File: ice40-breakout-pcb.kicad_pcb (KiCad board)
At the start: 2 copper layers, 55 parts, among them J1 USB_B_Micro, J2 USB_Break_Out, U1 SIT2001BI-S2-33E-12.000000G, U2 TLV73333PDBV, U3 TLV73312PDBV, U4 AT25SF081-SHD-X, U5 ICE40HX4K-TQ144

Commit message: Experimenting with external connector configuration.
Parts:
- added J3: Conn_02x16_Odd_Even, Connector_PinHeader_2.54mm:PinHeader_2x16_P2.54mm_Vertical, F.Cu at (94.8, 66.6)
- added J4: Conn_02x16_Odd_Even, Connector_PinHeader_2.54mm:PinHeader_2x16_P2.54mm_Vertical, F.Cu at (145.2, 104.7)
- added J5: Conn_02x16_Odd_Even, Connector_PinHeader_2.54mm:PinHeader_2x16_P2.54mm_Vertical, F.Cu at (139.1, 60.5)
- added J6: Conn_02x04_Odd_Even, Connector_PinHeader_2.54mm:PinHeader_2x04_P2.54mm_Vertical, F.Cu at (142.7, 123.5)
- moved R10 3.44 mm to (139.8, 111.2)
- moved C12 3.44 mm to (142.7, 111.2)
- moved R13 3.44 mm to (136.8, 111.2)
- moved R14 3.44 mm to (133.9, 111.2)
- moved U4 3.44 mm to (138.3, 116.8)
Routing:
- net +3V3: track 230.7 -> 343.2 mm
- net CDONE: track 14.3 -> 47.1 mm
- net CRESET: track 11.2 -> 41.9 mm
- net SPI_MISO: track 15.7 -> 40.0 mm
- net SPI_MOSI: track 24.5 -> 41.7 mm
- net SPI_SS: track 21.2 -> 37.8 mm
- net SPI_SCK: track 28.8 -> 43.2 mm
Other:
- board outline added: 56 x 78.1 mm

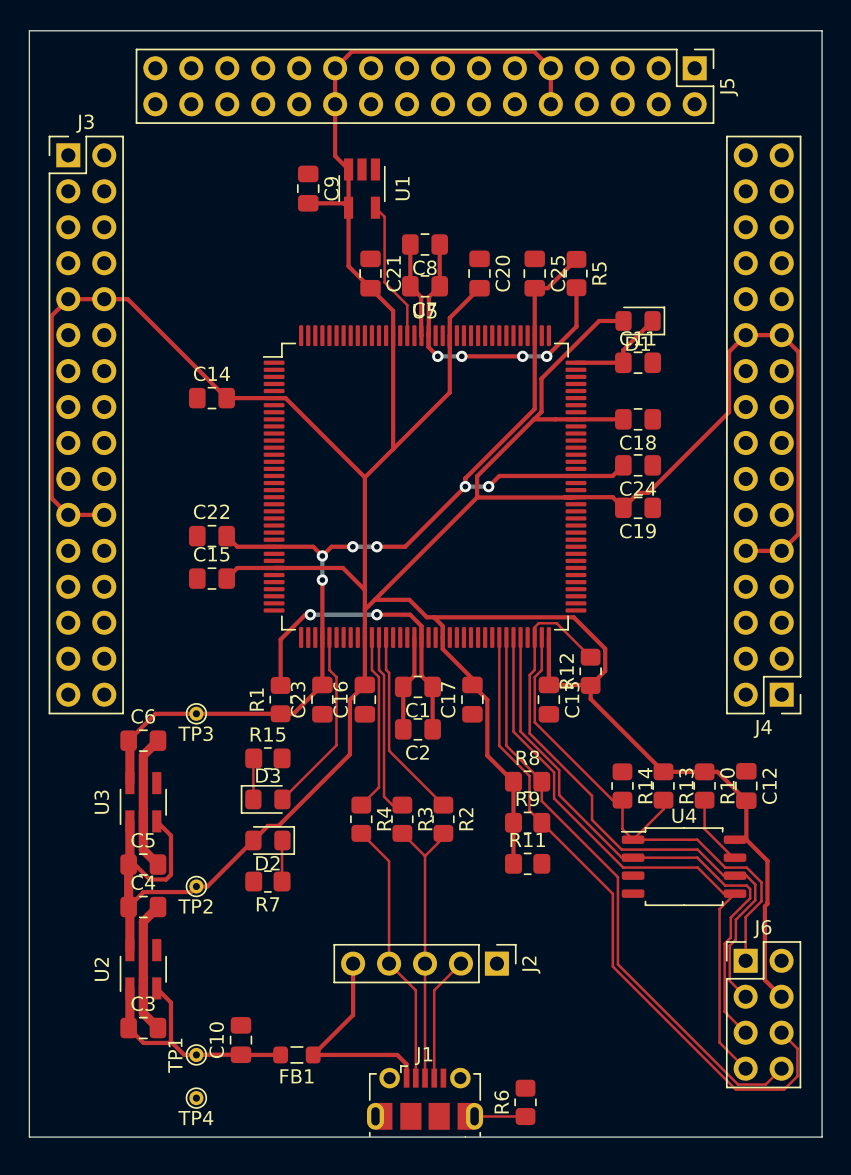
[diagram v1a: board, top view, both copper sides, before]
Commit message: Fine adjustment of board outline.
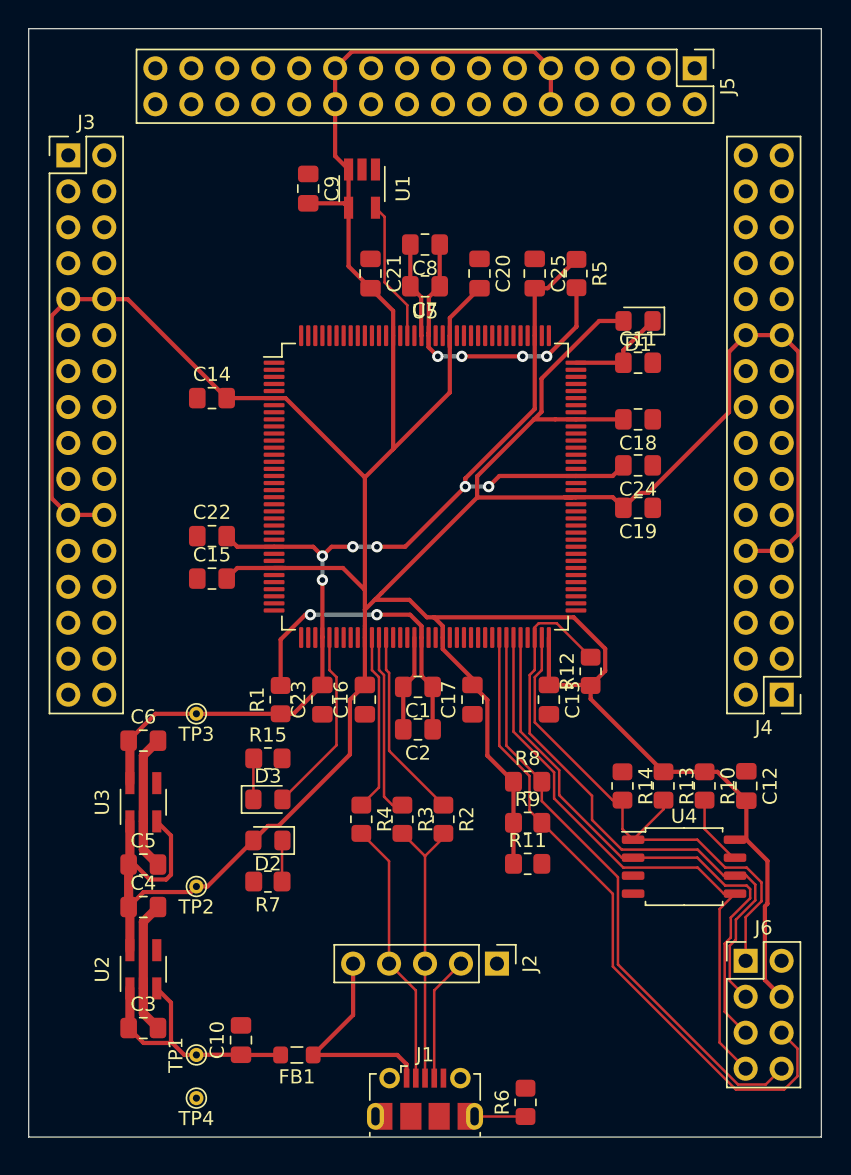
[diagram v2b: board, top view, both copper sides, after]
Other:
- board size 56 x 78.1 mm -> 56 x 78.3 mm

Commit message: Adjust power to make it easier to break out more signals.
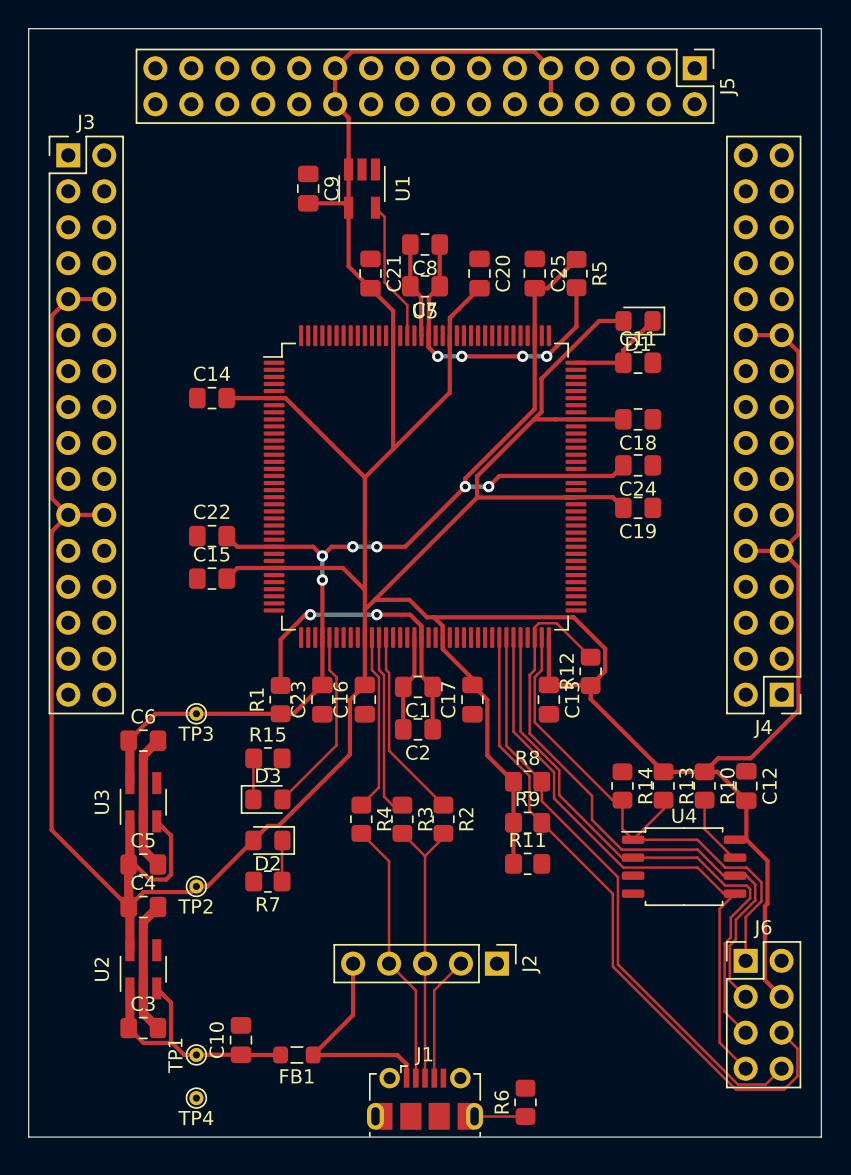
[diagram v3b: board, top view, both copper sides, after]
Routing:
- net +3V3: track 343.2 -> 366.1 mm
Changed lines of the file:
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@@
     (thickness 1.6)
     (drawings 4)
-    (tracks 349)
+    (tracks 350)
     (zones 0)
     (modules 59)
@@
   (segment (start 134.025 78.3) (end 132.302228 78.3) (width 0.3) (layer F.Cu) (net 3))
   (segment (start 113.65 60.45) (end 113.65 62.99) (width 0.3) (layer F.Cu) (net 3))
-  (segment (start 113.65 66.65) (end 114.6 67.6) (width 0.3) (layer F.Cu) (net 3))
-  (segment (start 113.65 62.99) (end 113.65 66.65) (width 0.3) (layer F.Cu) (net 3))
   (segment (start 114.830001 59.269999) (end 113.65 60.45) (width 0.3) (layer F.Cu) (net 3))
   (segment (start 127.709999 59.269999) (end 114.830001 59.269999) (width 0.3) (layer F.Cu) (net 3))
   (segment (start 128.89 60.45) (end 127.709999 59.269999) (width 0.3) (layer F.Cu) (net 3))
   (segment (start 128.89 62.99) (end 128.89 60.45) (width 0.3) (layer F.Cu) (net 3))
-  (segment (start 98.9975 76.76) (end 97.34 76.76) (width 0.3) (layer F.Cu) (net 3))
-  (segment (start 105.9875 83.75) (end 98.9975 76.76) (width 0.3) (layer F.Cu) (net 3))
   (segment (start 97.34 76.76) (end 94.8 76.76) (width 0.3) (layer F.Cu) (net 3))
   (segment (start 93.619999 77.940001) (end 93.619999 90.819999) (width 0.3) (layer F.Cu) (net 3))
@@
   (segment (start 145.2 79.3) (end 146.380001 80.480001) (width 0.3) (layer F.Cu) (net 3))
   (segment (start 142.66 94.54) (end 145.2 94.54) (width 0.3) (layer F.Cu) (net 3))
-  (segment (start 135.77527 90.44499) (end 141.479999 84.740261) (width 0.3) (layer F.Cu) (net 3))
-  (segment (start 141.479999 80.480001) (end 142.66 79.3) (width 0.3) (layer F.Cu) (net 3))
-  (segment (start 141.479999 84.740261) (end 141.479999 80.480001) (width 0.3) (layer F.Cu) (net 3))
-  (segment (start 135.06751 90.44499) (end 135.77527 90.44499) (width 0.3) (layer F.Cu) (net 3))
-  (segment (start 134.0125 91.5) (end 135.06751 90.44499) (width 0.3) (layer F.Cu) (net 3))
   (segment (start 131.7 105) (end 136.85 110.15) (width 0.3) (layer F.Cu) (net 3))
   (segment (start 131.7 104.05) (end 131.7 105) (width 0.3) (layer F.Cu) (net 3))
@@
   (segment (start 144.190031 119.471204) (end 144.009999 119.651236) (width 0.3) (layer F.Cu) (net 3))
   (segment (start 144.009999 124.859999) (end 145.19 126.04) (width 0.3) (layer F.Cu) (net 3))
+  (segment (start 114.6 63.94) (end 113.65 62.99) (width 0.3) (layer F.Cu) (net 3))
+  (segment (start 114.6 67.6) (end 114.6 63.94) (width 0.3) (layer F.Cu) (net 3))
+  (segment (start 93.619999 93.180001) (end 94.8 92) (width 0.3) (layer F.Cu) (net 3))
+  (segment (start 93.619999 114.257499) (end 93.619999 93.180001) (width 0.3) (layer F.Cu) (net 3))
+  (segment (start 99.0625 119.7) (end 93.619999 114.257499) (width 0.3) (layer F.Cu) (net 3))
+  (segment (start 146.380001 95.720001) (end 145.2 94.54) (width 0.3) (layer F.Cu) (net 3))
+  (segment (start 146.380001 105.814001) (end 146.380001 95.720001) (width 0.3) (layer F.Cu) (net 3))
+  (segment (start 142.999012 109.19499) (end 146.380001 105.814001) (width 0.3) (layer F.Cu) (net 3))
+  (segment (start 140.70501 109.19499) (end 142.999012 109.19499) (width 0.3) (layer F.Cu) (net 3))
+  (segment (start 139.75 110.15) (end 140.70501 109.19499) (width 0.3) (layer F.Cu) (net 3))
   (via (at 114.9 94.25) (size 0.8) (drill 0.4) (layers F.Cu B.Cu) (net 4))
   (via (at 116.6 94.25) (size 0.8) (drill 0.4) (layers F.Cu B.Cu) (net 4))

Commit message: Cosmetic tweak.
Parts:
- moved TP2 0.40 mm to (103.8, 118.7)
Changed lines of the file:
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@@
     (add_net VPP_2V5)
+  )
+  (module TestPoint:TestPoint_THTPad_D1.0mm_Drill0.5mm (layer F.Cu)
+    (at 103.85 118.65 180)
+    (descr "THT pad as test Point, diameter 1.0mm, hole diameter 0.5mm")
+    (tags "test point THT pad")
+    (attr virtual)
+    (fp_text reference TP2 (at 0 -1.448) (layer F.SilkS)
+      (effects (font (size 1 1) (thickness 0.15)))
+    )
+    (fp_text value TestPoint (at 0 1.55) (layer F.Fab)
+      (effects (font (size 1 1) (thickness 0.15)))
+    )
+    (fp_circle (center 0 0) (end 1 0) (layer F.CrtYd) (width 0.05))
+    (fp_circle (center 0 0) (end 0 0.7) (layer F.SilkS) (width 0.12))
+    (fp_text user %R (at 0 -1.45) (layer F.Fab)
+      (effects (font (size 1 1) (thickness 0.15)))
+    )
+    (pad 1 thru_hole circle (at 0 0 180) (size 1 1) (drill 0.5) (layers *.Cu *.Mask)
+      (net 3 +3V3))
   )
   (module Connector_PinHeader_2.54mm:PinHeader_2x04_P2.54mm_Vertical (layer F.Cu)
@@
     (pad 1 thru_hole circle (at 0 0 180) (size 1 1) (drill 0.5) (layers *.Cu *.Mask)
       (net 4 +1V2))
-  )
-  (module TestPoint:TestPoint_THTPad_D1.0mm_Drill0.5mm (layer F.Cu)
-    (at 103.85 118.25 180)
-    (descr "THT pad as test Point, diameter 1.0mm, hole diameter 0.5mm")
-    (tags "test point THT pad")
-    (attr virtual)
-    (fp_text reference TP2 (at 0 -1.448) (layer F.SilkS)
-      (effects (font (size 1 1) (thickness 0.15)))
-    )
-    (fp_text value TestPoint (at 0 1.55) (layer F.Fab)
-      (effects (font (size 1 1) (thickness 0.15)))
-    )
-    (fp_circle (center 0 0) (end 1 0) (layer F.CrtYd) (width 0.05))
-    (fp_circle (center 0 0) (end 0 0.7) (layer F.SilkS) (width 0.12))
-    (fp_text user %R (at 0 -1.45) (layer F.Fab)
-      (effects (font (size 1 1) (thickness 0.15)))
-    )
-    (pad 1 thru_hole circle (at 0 0 180) (size 1 1) (drill 0.5) (layers *.Cu *.Mask)
-      (net 3 +3V3))
   )
   (module TestPoint:TestPoint_THTPad_D1.0mm_Drill0.5mm (layer F.Cu)
@@
   (segment (start 100.55975 117.75501) (end 101.71525 117.75501) (width 0.3) (layer F.Cu) (net 3))
   (segment (start 99.0625 116.7) (end 99.50474 116.7) (width 0.3) (layer F.Cu) (net 3))
-  (segment (start 103.45501 118.64499) (end 103.85 118.25) (width 0.3) (layer F.Cu) (net 3))
-  (segment (start 100.11751 118.64499) (end 103.45501 118.64499) (width 0.3) (layer F.Cu) (net 3))
-  (segment (start 99.0625 119.7) (end 100.11751 118.64499) (width 0.3) (layer F.Cu) (net 3))
-  (segment (start 104.625 118.25) (end 107.875 115) (width 0.3) (layer F.Cu) (net 3))
-  (segment (start 103.85 118.25) (end 104.625 118.25) (width 0.3) (layer F.Cu) (net 3))
   (segment (start 120.13498 99.23498) (end 118.9 98) (width 0.3) (layer F.Cu) (net 3))
   (segment (start 116.45 98) (end 115.75 98.7) (width 0.3) (layer F.Cu) (net 3))
@@
   (segment (start 140.70501 109.19499) (end 142.999012 109.19499) (width 0.3) (layer F.Cu) (net 3))
   (segment (start 139.75 110.15) (end 140.70501 109.19499) (width 0.3) (layer F.Cu) (net 3))
+  (segment (start 107.5 115) (end 103.85 118.65) (width 0.3) (layer F.Cu) (net 3))
+  (segment (start 107.875 115) (end 107.5 115) (width 0.3) (layer F.Cu) (net 3))
+  (segment (start 100.11751 118.64499) (end 103.84499 118.64499) (width 0.3) (layer F.Cu) (net 3))
+  (segment (start 103.84499 118.64499) (end 103.85 118.65) (width 0.3) (layer F.Cu) (net 3))
+  (segment (start 99.0625 119.7) (end 100.11751 118.64499) (width 0.3) (layer F.Cu) (net 3))
   (via (at 114.9 94.25) (size 0.8) (drill 0.4) (layers F.Cu B.Cu) (net 4))
   (via (at 116.6 94.25) (size 0.8) (drill 0.4) (layers F.Cu B.Cu) (net 4))

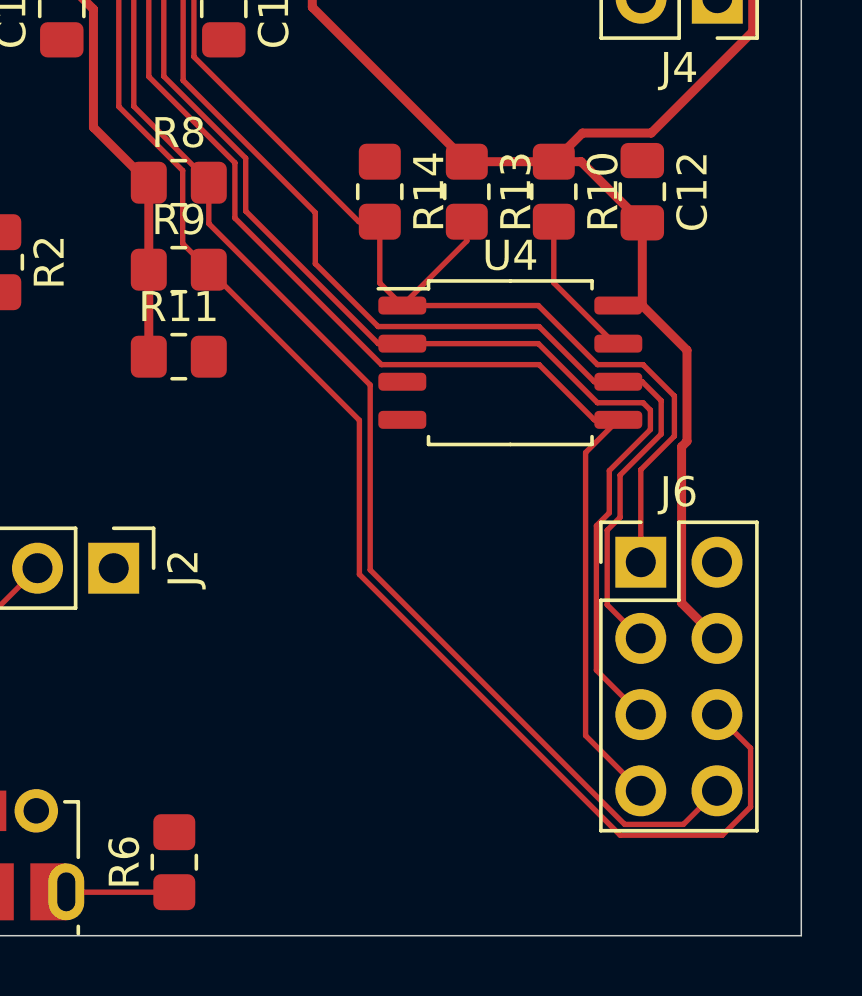
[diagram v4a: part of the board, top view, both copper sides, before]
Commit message: Move SPI connector to make room for mounting hole.
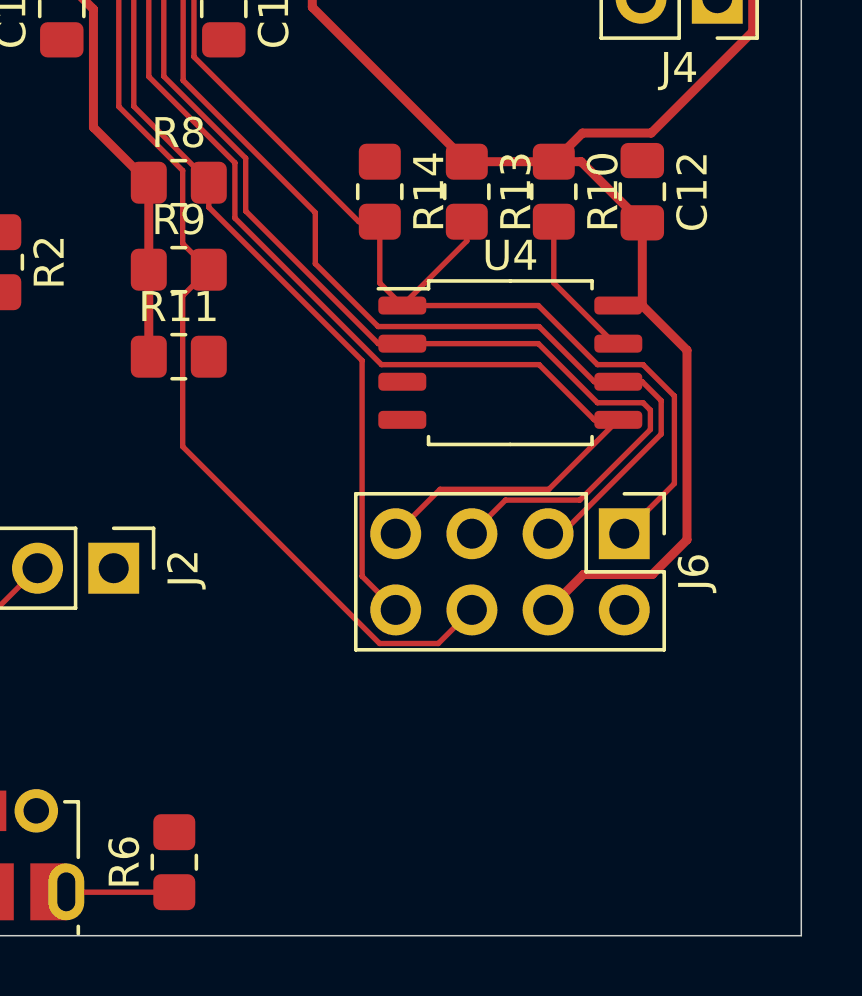
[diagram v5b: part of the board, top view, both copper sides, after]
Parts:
- moved J6 1.10 mm to (142.1, 122.5), turned to 270 degrees
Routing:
- net CRESET: track 41.9 -> 28.0 mm
- net CDONE: track 47.1 -> 33.4 mm
- net SPI_MOSI: track 41.7 -> 37.1 mm
- net SPI_MISO: track 40.0 -> 36.5 mm
- net SPI_SCK: track 43.2 -> 40.3 mm
- net +3V3: track 366.1 -> 367.8 mm
- net SPI_SS: track 37.8 -> 37.1 mm
